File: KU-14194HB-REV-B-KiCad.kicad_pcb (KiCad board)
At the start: 2 copper layers, 387.7 x 180.3 mm, 167 parts, among them CN1 KEYBOARD_20PIN_MALE, CN10 LED_CONNECTOR, CN2 USER_PORT_CON, CN3 CASSETTE_PORT_CON, CN4 SERIAL_BUS_CON, CN6 EXPANSION_PORT, CN7 POWER_CON, CN8 CONTROL_PORT, CN9 CONTROL_PORT, Q1 2SC1815, Q2 2SC1815, Q3 TP298/2SD880, Q7 2SC1815, SW1 POWER_SWITCH, U1 CIA_U1, U10 4164-2, U11 4164-2, U12 4164-2, U13 74LS257, U15 74LS139, U17 PLA_U17, U2 CIA_U2, U20 556, U21 4164-2, U22 4164-2, U23 4164-2, U24 4164-2, U25 74LS257, U27 7408_U27, U28 4066_U28, U29 74LS74, U3 2364A, U30 74LS193, U31 74LS629N, U32 MC4044, U4 2364A, U5 2332A, U7 6510_MPU, U8 7406N, U9 4164-2, Y1 Crystal

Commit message: Almost done now
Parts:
- added C10: 470pF, KU-14194HB-RevB-KiCad:CAP_AXIAL_P10.16mm, F.Cu at (210.8, 127.0)
- added C101: .1, KU-14194HB-RevB-KiCad:CAP_P5.08mm, F.Cu at (271.8, 132.1)
- added C11: 470pF, KU-14194HB-RevB-KiCad:CAP_AXIAL_P10.16mm, F.Cu at (210.8, 139.7)
- added C12: 10uF, KU-14194HB-RevB-KiCad:CAP_ELYT_RADIAL_P2.54mm, F.Cu at (233.7, 114.3)
- added C13: 10uF, KU-14194HB-RevB-KiCad:CAP_ELYT_RADIAL_P2.54mm, F.Cu at (241.3, 114.3)
- added C15: 10uF, KU-14194HB-RevB-KiCad:CAP_ELYT_RADIAL_P2.54mm, F.Cu at (299.7, 111.8)
- added C16: .1, KU-14194HB-RevB-KiCad:CAP_P5.08mm, F.Cu at (294.6, 106.7)
- added C30: .1, KU-14194HB-RevB-KiCad:CAP_P5.08mm, F.Cu at (139.7, 170.2)
- added C32: .1, KU-14194HB-RevB-KiCad:CAP_P5.08mm, F.Cu at (172.7, 170.2)
- added C34: 10uF, KU-14194HB-RevB-KiCad:CAP_ELYT_RADIAL_P2.54mm, F.Cu at (200.7, 218.4)
- added C37: 1000pF, KU-14194HB-RevB-KiCad:CAP_P5.08mm, F.Cu at (238.8, 134.6)
- added C45: .1, KU-14194HB-RevB-KiCad:CAP_P5.08mm, F.Cu at (139.7, 208.3)
- added C48: 1800pF, KU-14194HB-RevB-KiCad:RESISTOR_10.16mm, F.Cu at (233.7, 190.5)
- added C49: .1, KU-14194HB-RevB-KiCad:CAP_P12mm, F.Cu at (213.4, 182.9)
- added C50: .1, KU-14194HB-RevB-KiCad:CAP_P5.08mm, F.Cu at (215.9, 170.2)
- added C51: .1, KU-14194HB-RevB-KiCad:CAP_P5.08mm, F.Cu at (226.1, 170.2)
- added C52: .1, KU-14194HB-RevB-KiCad:CAP_P12mm, F.Cu at (218.4, 195.6)
- added C53: .1, KU-14194HB-RevB-KiCad:CAP_P5.08mm, F.Cu at (256.5, 208.3)
- added C54: .1, KU-14194HB-RevB-KiCad:CAP_P5.08mm, F.Cu at (256.5, 221.0)
- added C60: .1, KU-14194HB-RevB-KiCad:CAP_P5.08mm, F.Cu at (254.0, 127.0)
- added C62: 10uF, KU-14194HB-RevB-KiCad:CAP_ELYT_RADIAL_P2.54mm, F.Cu at (236.2, 221.0)
- added C7: .1, KU-14194HB-RevB-KiCad:CAP_P5.08mm, F.Cu at (177.8, 76.2)
- added C80: NC, KU-14194HB-RevB-KiCad:CAP_AXIAL_P12.7mm, F.Cu at (281.9, 157.5)
- added C93: 1800pF, KU-14194HB-RevB-KiCad:RESISTOR_10.16mm, F.Cu at (228.6, 190.5)
- added C94: 10uF, KU-14194HB-RevB-KiCad:CAP_ELYT_RADIAL_P2.54mm, F.Cu at (243.8, 208.3)
- added FB10: FERRITE_BEAD, KU-14194HB-RevB-KiCad:FERRITE_BEAD_TH_P12.7mm, F.Cu at (208.3, 189.2)
- added FB11: FERRITE_BEAD, KU-14194HB-RevB-KiCad:FERRITE_BEAD_TH_P12.7mm, F.Cu at (223.5, 189.2)
- added FB12: FERRITE_BEAD, KU-14194HB-RevB-KiCad:FERRITE_BEAD_TH_P12.7mm, F.Cu at (251.5, 214.6)
- added FB13: FERRITE_BEAD, KU-14194HB-RevB-KiCad:FERRITE_BEAD_TH_P12.7mm, F.Cu at (227.3, 121.9)
- added FB14: FERRITE_BEAD, KU-14194HB-RevB-KiCad:FERRITE_BEAD_TH_P12.7mm, F.Cu at (276.9, 163.8)
- added FB15: FERRITE_BEAD, KU-14194HB-RevB-KiCad:FERRITE_BEAD_TH_P12.7mm, F.Cu at (276.9, 179.1)
- added FB22: FERRITE_BEAD, KU-14194HB-RevB-KiCad:FERRITE_BEAD_TH_P12.7mm, F.Cu at (265.4, 127.0)
- added FB23: FERRITE_NARROW, KU-14194HB-RevB-KiCad:FERRITE_BEAD_TH_P12.7mm, F.Cu at (266.7, 214.6)
- added Q8: 2SC1815, KU-14194HB-RevB-KiCad:Q_NPN_ECB, F.Cu at (251.5, 200.7)
- added R38: 1K, KU-14194HB-RevB-KiCad:RESISTOR, F.Cu at (238.8, 170.2)
- added R6: 1K, KU-14194HB-RevB-KiCad:RESISTOR, F.Cu at (221.0, 127.0)
- added R7: 10K, KU-14194HB-RevB-KiCad:RESISTOR, F.Cu at (236.2, 134.6)
- added U14: 74LS258, KU-14194HB-RevB-KiCad:DIP16, F.Cu at (138.4, 156.2)
- added U16: 4066_U28, KU-14194HB-RevB-KiCad:DIP14, F.Cu at (174.0, 157.5)
- added U18: 6581, KU-14194HB-RevB-KiCad:DIP28, F.Cu at (223.5, 148.6)
- added U19: VIC, KU-14194HB-RevB-KiCad:DIP40, F.Cu at (264.2, 160.0)
- added U26: 74LS373, KU-14194HB-RevB-KiCad:DIP20, F.Cu at (138.4, 191.8)
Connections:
- net PHI_0 renamed PHI0
- CN6 pad 6: Net-(CN6-Pad6) -> DOT_CLOCK
- U17 pad 5: ~VA14~ -> ~CHAREN~
- U2 pad 2: ~VA14~ -> ~CHAREN~
- U27 pad 10: (no net) -> /Sheet5D659BBD/AEC
- U27 pad 8: (no net) -> Net-(U27-Pad8)
- U27 pad 9: (no net) -> /Sheet5D659BBD/~COLOR~
- U8 pad 11: ~VA14~ -> /Sheet5D659BBD/AEC
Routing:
- net (no net): track 3397.0 -> 862.8 mm, vias 156 -> 45
- net ~VA14~: track 351.6 -> 0.00 mm, vias 8 -> 0
- net Net-(C12-Pad2): track 0.00 -> 350.2 mm
- net Net-(C97-Pad2): track 373.9 -> 23.7 mm
- net D7: track 531.3 -> 861.7 mm, vias 9 -> 7
- net ~CHAREN~: track 104.8 -> 315.0 mm, vias 2 -> 5
- net Net-(U16-Pad2): track 0.00 -> 191.9 mm, vias 0 -> 8
- net Net-(U16-Pad3): track 0.00 -> 189.6 mm, vias 0 -> 7
- net Net-(U16-Pad10): track 0.00 -> 176.5 mm, vias 0 -> 5
- net Net-(U16-Pad9): track 0.00 -> 172.1 mm, vias 0 -> 4
- net /Sheet5D659BBD/VA6': track 0.00 -> 150.0 mm, vias 0 -> 2
- net /Sheet5D659BBD/AEC: track 206.2 -> 347.7 mm, vias 11 -> 9
- net /Sheet5D659BBD/VA7': track 0.00 -> 138.7 mm, vias 0 -> 2
- net Net-(U27-Pad8): track 0.00 -> 117.9 mm, vias 0 -> 3
- net /Sheet5D659BBD/AUDIO_OUT: track 0.00 -> 109.9 mm, vias 0 -> 3
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
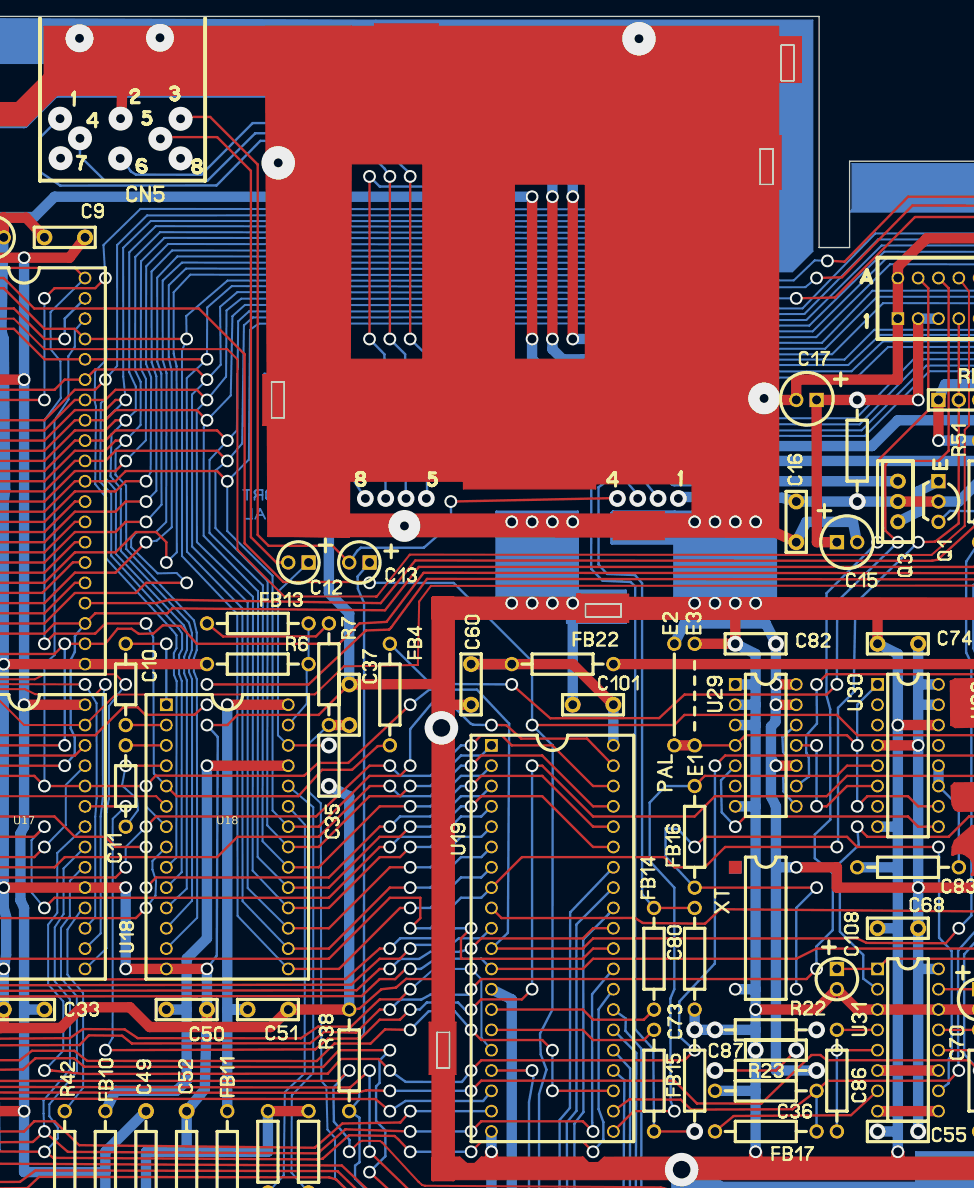
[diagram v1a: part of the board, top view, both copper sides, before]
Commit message: AV connector, Not used parts, pdf update
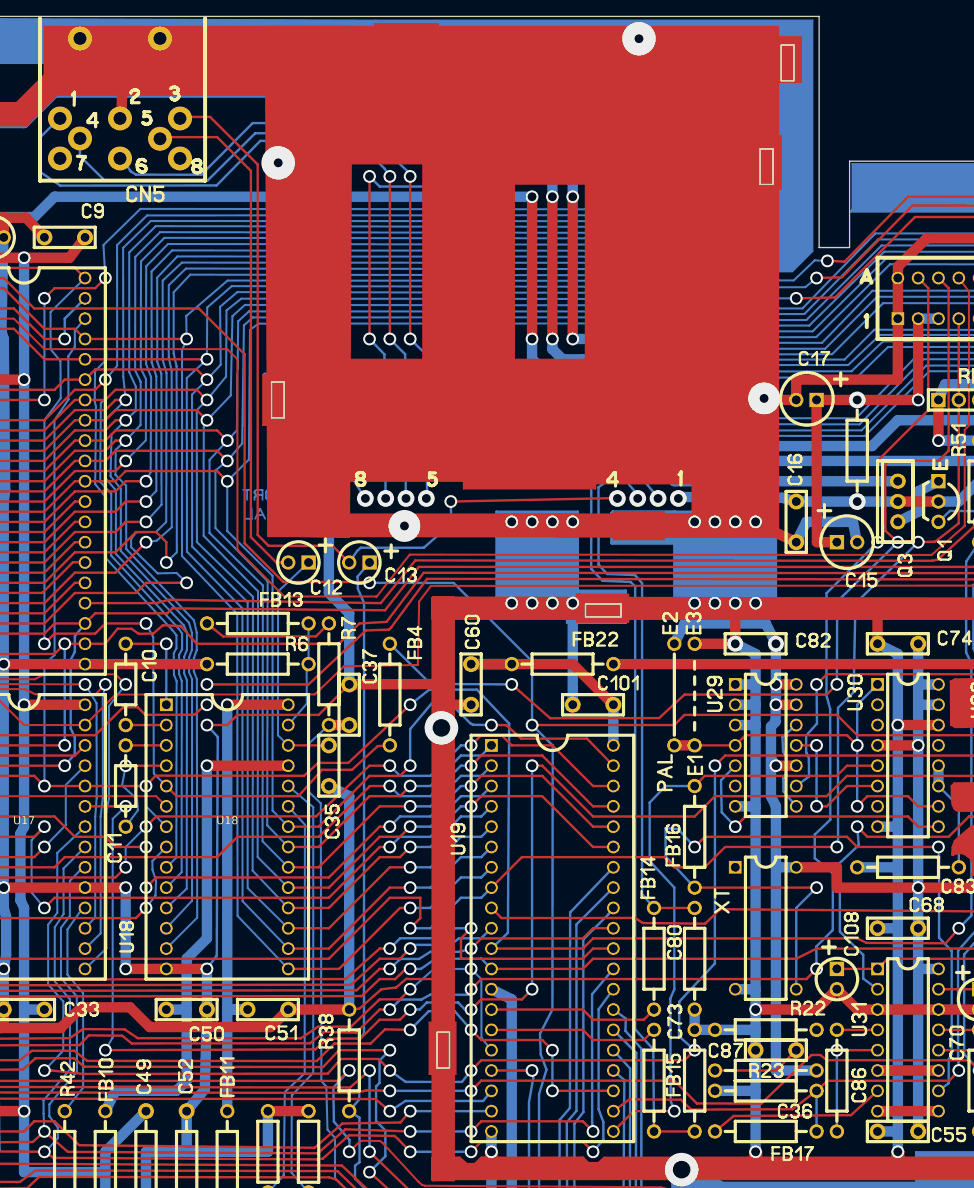
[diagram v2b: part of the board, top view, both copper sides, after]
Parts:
- added C35: NC, KU-14194HB-RevB-KiCad:CAP_P5.08mm, F.Cu at (236.2, 137.2)
- added C55: NC, KU-14194HB-RevB-KiCad:CAP_P5.08mm, F.Cu at (309.9, 185.4)
- added C73: NC, KU-14194HB-RevB-KiCad:CAP_AXIAL_P12.7mm, F.Cu at (281.9, 185.4)
- added C87: NC, KU-14194HB-RevB-KiCad:CAP_P5.08mm, F.Cu at (294.6, 175.3)
- added CN5: AV_CONN, KU-14194HB-RevB-KiCad:AV_CON_DIN8, F.Cu at (210.1, 58.8)
- added R22: NC, KU-14194HB-RevB-KiCad:RESISTOR, F.Cu at (297.2, 172.7)
- added R23: NC, KU-14194HB-RevB-KiCad:RESISTOR, F.Cu at (297.2, 177.8)
- added XT1: NOT USED, KU-14194HB-RevB-KiCad:DIP4_DIP14_but_4_pins, F.Cu at (290.8, 160.0)
- C37: value 1000pF -> NC
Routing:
- net (no net): track 862.8 -> 567.4 mm, vias 45 -> 26
- net /Sheet5D659BBD/LUMA: track 101.5 -> 199.1 mm, vias 2 -> 4
- net /Sheet5D659BBD/CHROMA: track 68.5 -> 164.3 mm, vias 1 -> 4
- net /Sheet5D659BBD/COMP: track 0.00 -> 90.6 mm, vias 0 -> 3
- net Net-(C87-Pad1): track 0.00 -> 11.2 mm
- net Earth: track 6038.4 -> 6042.5 mm, vias 73 -> 68
- net Net-(C12-Pad1): track 34.1 -> 30.1 mm, vias 1 -> 0
- net Net-(FB16-Pad1): vias 4 -> 3
- net /Sheet5D659BBD/AUDIO_OUT: vias 3 -> 2
- net /Sheet5D659BBD/AUDIO_IN: vias 1 -> 0
- net /Sheet1/JOYA3: vias 3 -> 2
- net /Sheet1/+Vc: vias 11 -> 7

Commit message: Polygons to fill zones. Reducing DRC errors.
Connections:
- U31 pad 11: (no net) -> Earth
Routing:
- net Earth: track 6042.5 -> 4286.5 mm, vias 68 -> 93
- net Net-(C12-Pad2): track 350.2 -> 0.00 mm
- net D7: track 861.7 -> 531.3 mm
- net (no net): track 567.4 -> 290.6 mm, vias 26 -> 1
- added copper zone on B.Cu, net Earth
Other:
- outline, holes or cut-outs redrawn

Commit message: Replica 1.0
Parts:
- added M1: MODULATOR_LONGBOARD, KU-14194HB-RevB-KiCad:MODULATOR_PORT_LONGBOARD, F.Cu at (272.3, 106.3)
- added U6: 2114, KU-14194HB-RevB-KiCad:DIP18, F.Cu at (174.0, 94.0)
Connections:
- C102 pad 1: /Sheet1/CAN+5V -> CAN+5V
- C103 pad 1: /Sheet1/CAN+5V -> CAN+5V
- C63 pad 1: /Sheet1/CAN+5V -> CAN+5V
- C64 pad 1: /Sheet1/CAN+5V -> CAN+5V
- C65 pad 1: /Sheet1/CAN+5V -> CAN+5V
- C66 pad 1: /Sheet1/CAN+5V -> CAN+5V
- CN1 pad 8: BTNA\LP -> BTNA\~LP~
- CN5 pad 1: /Sheet5D659BBD/LUMA -> /Sheet5D659BBD/LUMA_O
- CN5 pad 4: /Sheet5D659BBD/COMP -> /Sheet5D659BBD/COMP_O
- CN5 pad 6: /Sheet5D659BBD/CHROMA -> /Sheet5D659BBD/CHROMA_O
- CN9 pad 6: BTNA\LP -> BTNA\~LP~
- FB22 pad 2: /Sheet5D659BBD/CAN+5V -> CAN+5V
- L1 pad 1: /Sheet1/CAN+5V -> CAN+5V
- L2 pad 1: /Sheet1/CAN+5V -> CAN+5V
- U1 pad 14: BTNA\LP -> BTNA\~LP~
- U13 pad 8: (no net) -> Earth
- U14 pad 2: ~CHAREN~ -> ~VA14~
- U17 pad 13: Net-(U17-Pad13) -> /Sheet5D659BBD/GR\~W~
- U17 pad 20: Net-(U17-Pad20) -> /Sheet5D659BBD/VA4
- U17 pad 21: Net-(U17-Pad21) -> /Sheet5D659BBD/VA5
- U17 pad 28: (no net) -> +5V
- U17 pad 5: ~CHAREN~ -> ~VA14~
- U2 pad 2: ~CHAREN~ -> ~VA14~
- U25 pad 8: (no net) -> Earth
- VR2 pad 2: /Sheet1/CAN+5V -> CAN+5V
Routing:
- net +5V: track 3855.6 -> 2728.5 mm, vias 57 -> 56
- net Earth: track 4286.5 -> 3386.1 mm, vias 93 -> 98
- net BTNA\~LP~: track 0.00 -> 731.1 mm, vias 0 -> 5
- net BTNA\LP: track 731.1 -> 0.00 mm, vias 5 -> 0
- net ~VA14~: track 0.00 -> 210.2 mm, vias 0 -> 3
- net ~CHAREN~: track 315.0 -> 104.8 mm, vias 5 -> 2
- net CAN+5V: track 0.00 -> 175.3 mm, vias 0 -> 3
- net /Sheet1/CAN+5V: track 175.3 -> 0.00 mm, vias 3 -> 0
- net (no net): track 290.6 -> 154.6 mm, vias 1 -> 8
- net /Sheet5D659BBD/LUMA_O: track 0.00 -> 97.6 mm, vias 0 -> 2
- net /Sheet5D659BBD/LUMA: track 199.1 -> 101.5 mm, vias 4 -> 0
- net /Sheet5D659BBD/CHROMA_O: track 0.00 -> 95.8 mm, vias 0 -> 2
- net /Sheet5D659BBD/CHROMA: track 164.3 -> 68.5 mm, vias 4 -> 0
- net /Sheet5D659BBD/COMP_O: track 0.00 -> 90.6 mm, vias 0 -> 2
- net /Sheet5D659BBD/COMP: track 90.6 -> 0.00 mm, vias 3 -> 0
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- added copper zone on B.Cu, net (none)
- added copper zone on F.Cu, net (none)
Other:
- board size 387.7 x 180.3 mm -> 388.6 x 180.3 mm
- board text added: "Replica 1.0 by BWACK 2019"
